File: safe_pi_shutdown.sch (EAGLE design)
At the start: 32 parts, among them IC1 MCP73831, IC2 LTC2952CF, IC3 MT3608, Q1 IRF7342, Q2 IRF7342, X4 22-27-2021-02

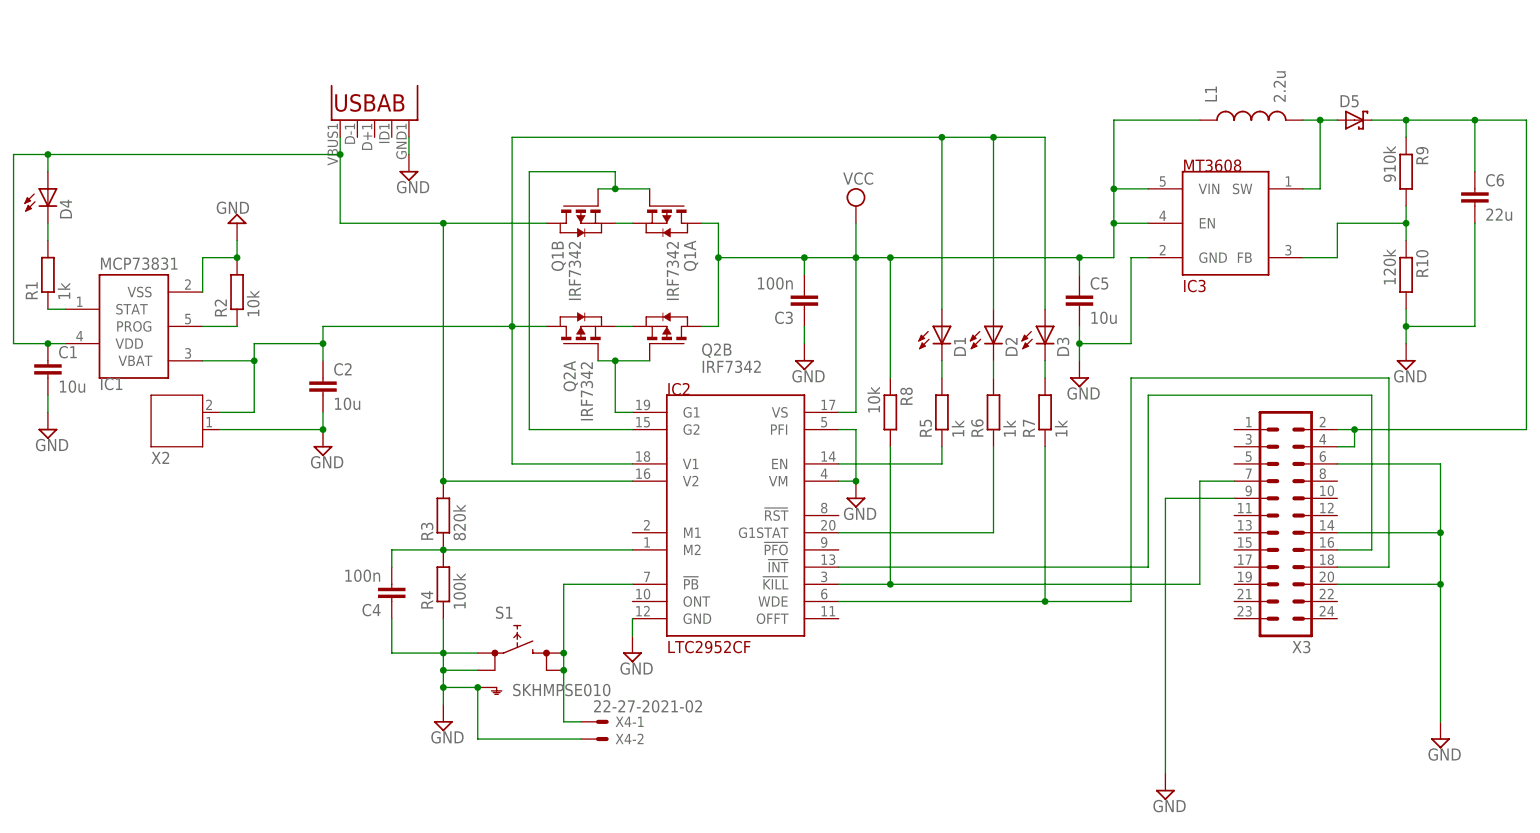
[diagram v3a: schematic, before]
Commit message: dodanie headerow do podlaczenia do plyty bazowej
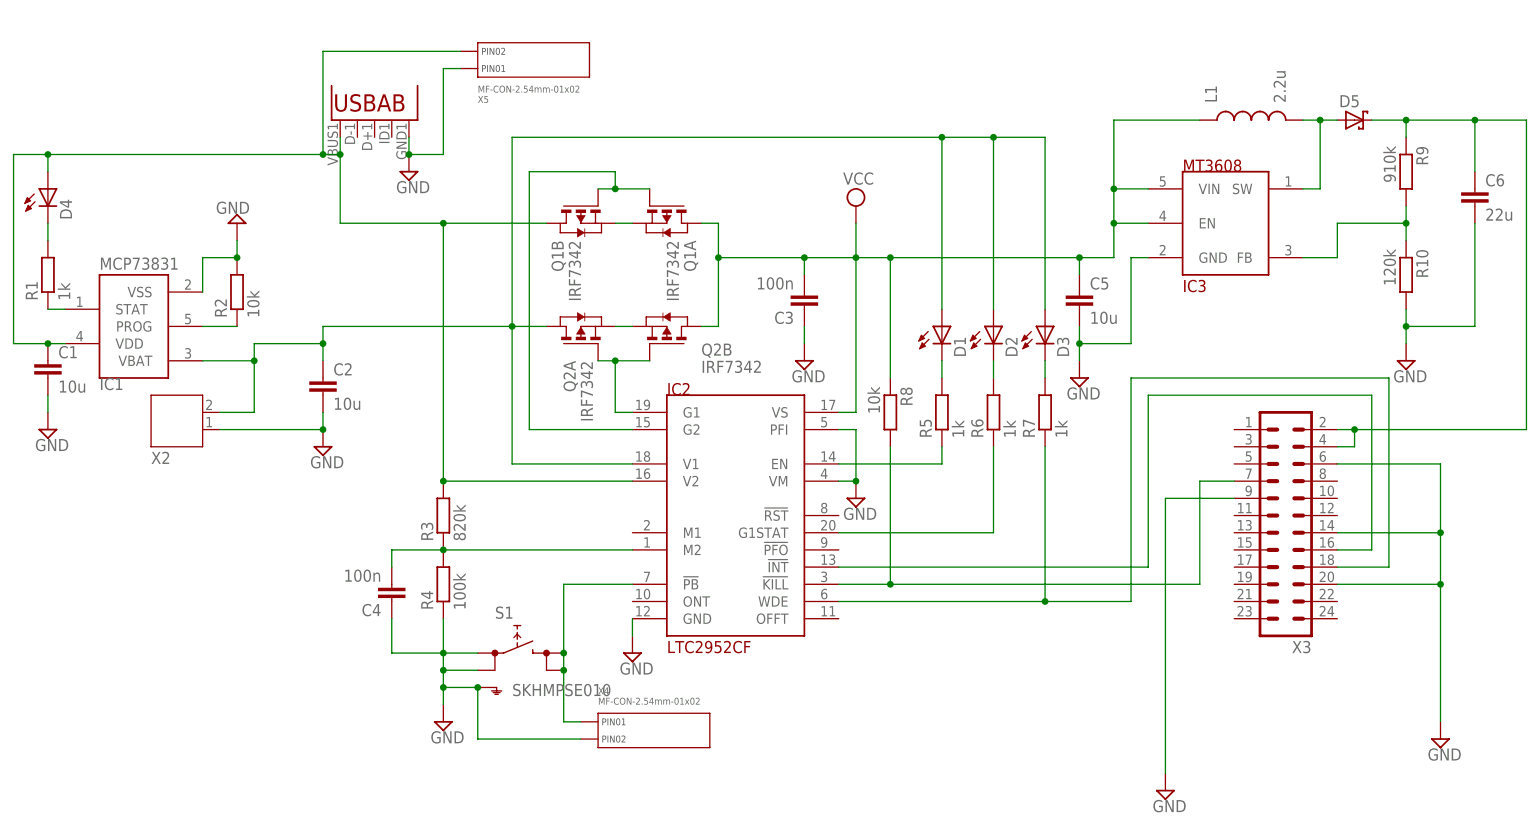
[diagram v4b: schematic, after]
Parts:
- added X5: MF-CON-2.54mm-01x02, MF_Connectors:CON_01X02_PTH_2.54MM
- X4: value 22-27-2021-02 -> MF-CON-2.54mm-01x02; device con-molex:22-27-2021-02 -> MF_Connectors:CON_01X02_PTH_2.54MM
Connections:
- net GND: now also X4.PIN2, X5.PIN1; no longer X4-2.S
- net N$5: now also X4.PIN1; no longer X4-1.S
- net V2: now also X5.PIN2
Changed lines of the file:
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@@
 <part name="IC1" library="mcp73831" deviceset="MCP73831" device=""/>
 <part name="SUPPLY14" library="supply2" deviceset="GND" device=""/>
-<part name="X4" library="con-molex" deviceset="22-?-02" device="27-2021"/>
 <part name="X3" library="con-lstb" deviceset="MA12-2" device=""/>
+<part name="X5" library="MF_Connectors" deviceset="CON_01X02" device="_PTH_2.54MM" value="MF-CON-2.54mm-01x02"/>
+<part name="X4" library="MF_Connectors" deviceset="CON_01X02" device="_PTH_2.54MM" value="MF-CON-2.54mm-01x02"/>
 </parts>
 <sheets>
@@
 <instance part="IC1" gate="G$1" x="22.86" y="139.7" rot="MR180"/>
 <instance part="SUPPLY14" gate="GND" x="10.16" y="124.46"/>
-<instance part="X4" gate="-1" x="91.44" y="81.28"/>
-<instance part="X4" gate="-2" x="91.44" y="78.74"/>
 <instance part="X3" gate="1" x="193.04" y="111.76" rot="R180"/>
+<instance part="X5" gate="G$1" x="73.66" y="177.8" rot="MR180"/>
+<instance part="X4" gate="G$1" x="91.44" y="81.28"/>
 </instances>
 <busses>
@@
 <wire x1="63.5" y1="167.64" x2="63.5" y2="165.1" width="0.1524" layer="91"/>
 <pinref part="SUPPLY1" gate="GND" pin="GND"/>
+<wire x1="63.5" y1="165.1" x2="68.58" y2="165.1" width="0.1524" layer="91"/>
+<wire x1="68.58" y1="165.1" x2="68.58" y2="177.8" width="0.1524" layer="91"/>
+<junction x="63.5" y="165.1"/>
+<pinref part="X5" gate="G$1" pin="PIN1"/>
+<wire x1="68.58" y1="177.8" x2="71.12" y2="177.8" width="0.1524" layer="91"/>
 </segment>
 <segment>
@@
 <wire x1="73.66" y1="78.74" x2="73.66" y2="86.36" width="0.1524" layer="91"/>
 <junction x="73.66" y="86.36"/>
-<pinref part="X4" gate="-2" pin="S"/>
+<pinref part="X4" gate="G$1" pin="PIN2"/>
 </segment>
 <segment>
@@
 <pinref part="D4" gate="G$1" pin="A"/>
 <wire x1="10.16" y1="162.56" x2="10.16" y2="165.1" width="0.1524" layer="91"/>
-<wire x1="10.16" y1="165.1" x2="53.34" y2="165.1" width="0.1524" layer="91"/>
+<wire x1="10.16" y1="165.1" x2="50.8" y2="165.1" width="0.1524" layer="91"/>
 <pinref part="IC1" gate="G$1" pin="VDD"/>
 <pinref part="C1" gate="G$1" pin="1"/>
+<wire x1="50.8" y1="165.1" x2="53.34" y2="165.1" width="0.1524" layer="91"/>
 <wire x1="12.7" y1="137.16" x2="10.16" y2="137.16" width="0.1524" layer="91"/>
 <wire x1="10.16" y1="137.16" x2="5.08" y2="137.16" width="0.1524" layer="91"/>
@@
 <junction x="10.16" y="165.1"/>
 <junction x="10.16" y="137.16"/>
+<wire x1="50.8" y1="165.1" x2="50.8" y2="180.34" width="0.1524" layer="91"/>
+<junction x="50.8" y="165.1"/>
+<pinref part="X5" gate="G$1" pin="PIN2"/>
+<wire x1="50.8" y1="180.34" x2="71.12" y2="180.34" width="0.1524" layer="91"/>
 </segment>
 </net>
@@
 <junction x="86.36" y="88.9"/>
 <junction x="86.36" y="91.44"/>
-<pinref part="X4" gate="-1" pin="S"/>
-</segment>
-</net>
+<pinref part="X4" gate="G$1" pin="PIN1"/>
+</segment>
+</net>

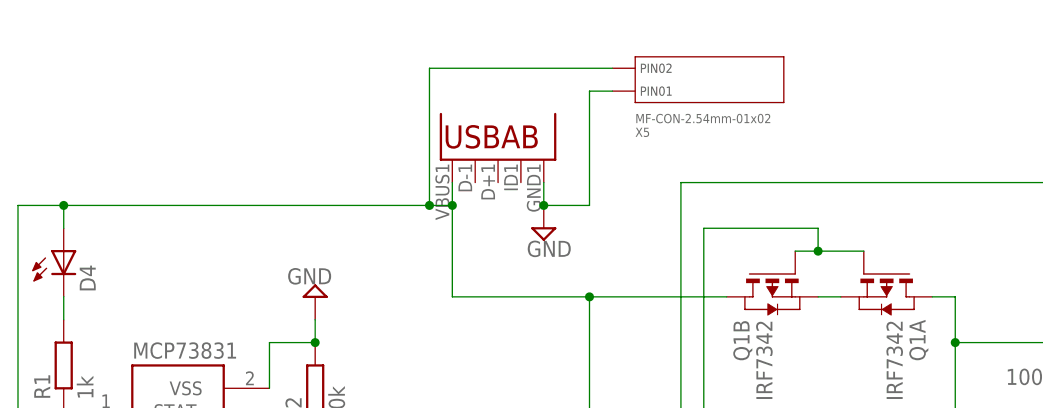
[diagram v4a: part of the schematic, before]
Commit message: zmiana micro usb, poprawki z kondensatorami i inne
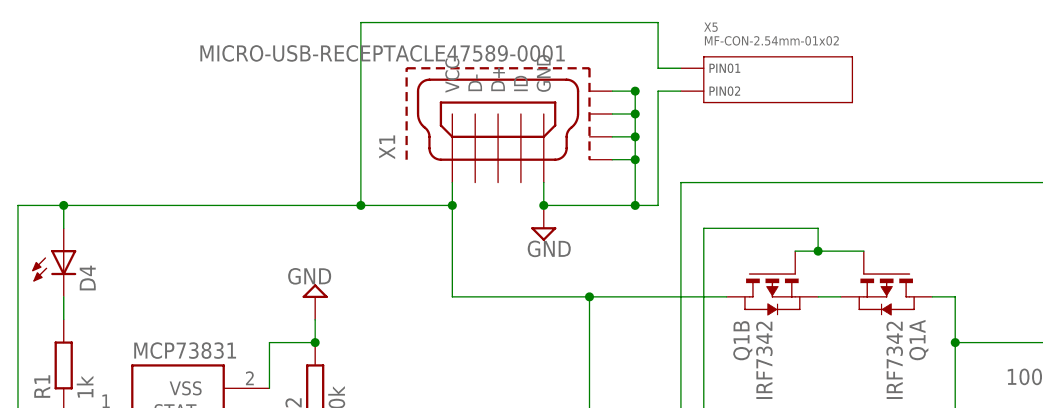
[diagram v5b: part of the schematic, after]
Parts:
- C5, C6: device rcl:C-EUC0603 -> rcl:C-EUC1206
- X1: value (none) -> MICRO-USB-RECEPTACLE47589-0001; device MicroUSB:USB"" -> con-molex-usb:MICRO-USB-RECEPTACLE47589-0001
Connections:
- net GND: now also X1.GND1, X1.GND2, X1.GND3, X1.GND4, X5.PIN2; no longer X5.PIN1
- net V2: now also X1.VCC, X5.PIN1; no longer X1.VBUS, X5.PIN2
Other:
- moved on the sheet: X5

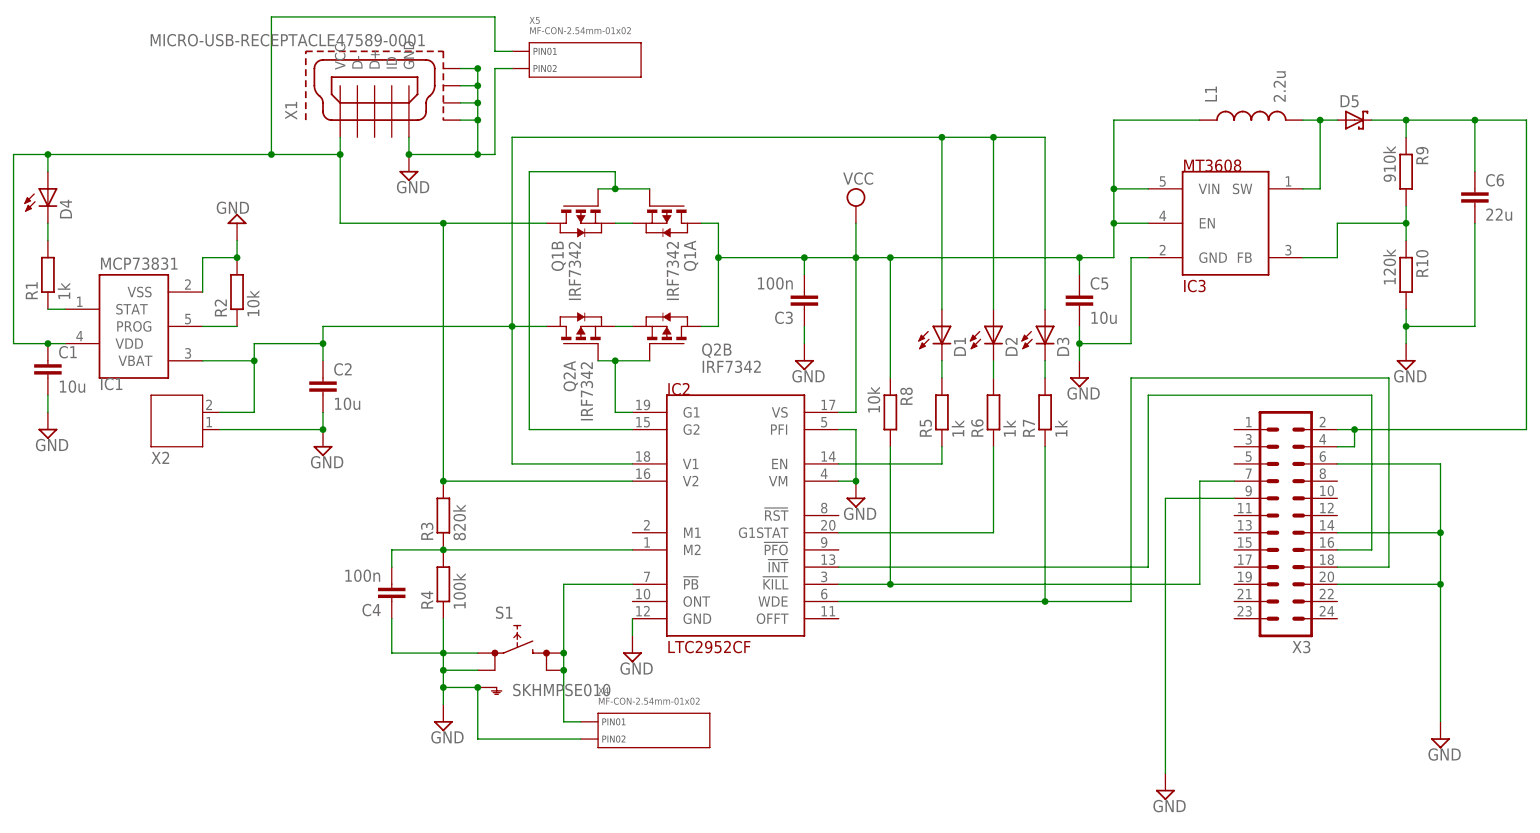
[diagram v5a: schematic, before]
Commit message: dodanie pull-up dla pinu INT
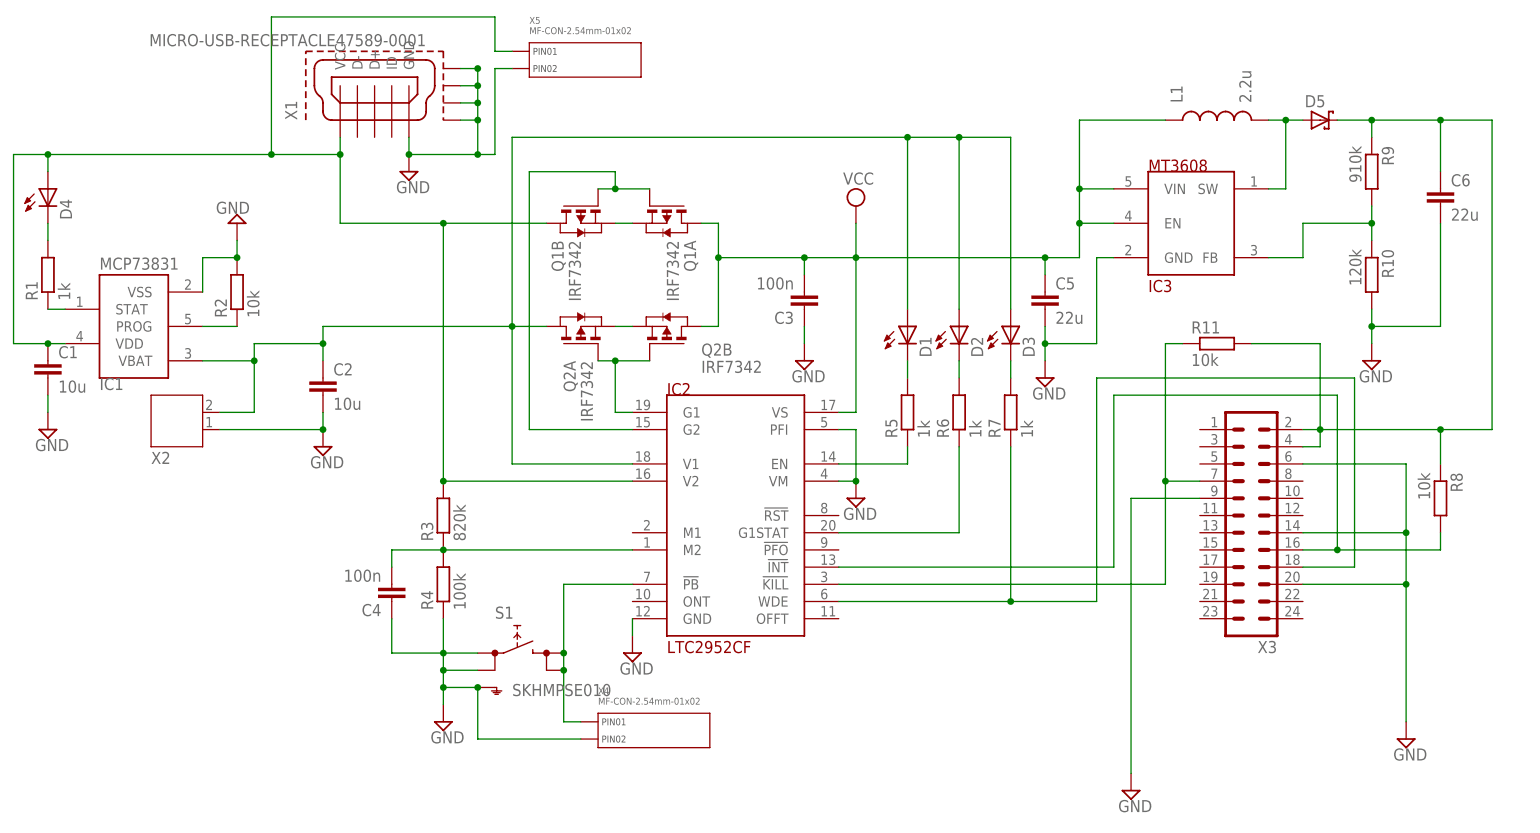
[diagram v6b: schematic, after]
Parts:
- added R11: 10k, rcl:R-EU_R0603
- C5: value 10u -> 22u
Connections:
- net N$10: now also R8.2
- net N$12: now also R11.1; no longer R8.2
- net N$4: now also R11.2, R8.1
- net VCC: no longer R8.1
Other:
- moved on the sheet: C5, C6, D1, D2, D3, D5, IC3, L1, R10, R5, R6, R7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

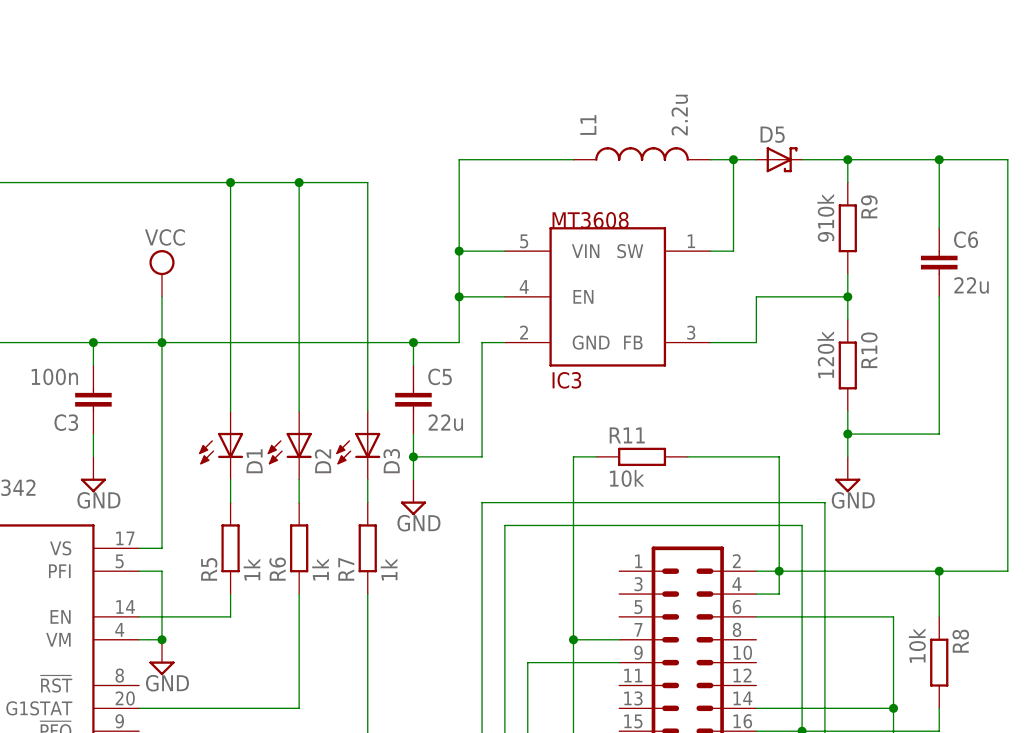
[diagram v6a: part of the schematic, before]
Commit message: boost converter changed to MIC2876
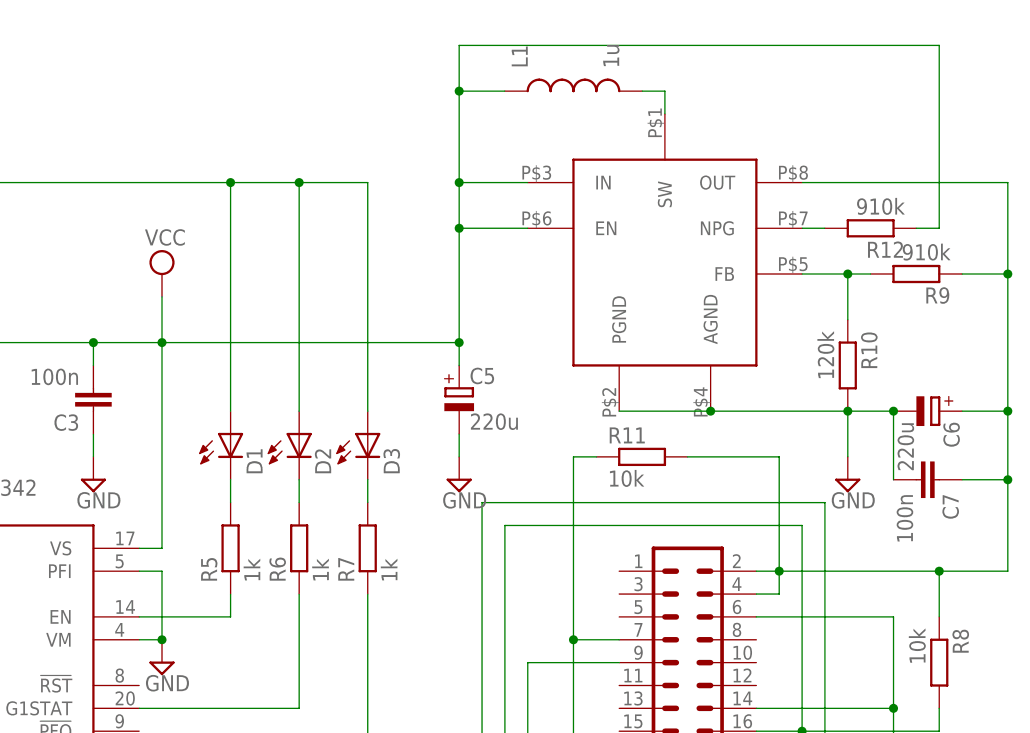
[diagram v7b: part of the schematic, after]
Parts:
- removed D5: (no value), eagle-ltspice:SCHOTTKY-DIODE
- added C7: 100n, rcl:C-EUC0402
- added R12: 910k, rcl:R-EU_R0603
- C5, C6: value 22u -> 220u; device rcl:C-EUC1206 -> rcl:CPOL-EUE3.5-8
- IC3: value MT3608 -> MIC2876; device mt3608:MT3608 -> mic2876:MIC2876
- L1: value 2.2u -> 1u; device SparkFun-Passives:INDUCTORDR1030 -> SparkFun-Passives:INDUCTORCR54-KIT
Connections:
- removed net N$13: D5.C, IC3.SW, L1.2
- new net N$11: IC3.NPG, R12.2
- new net N$9: IC3.SW, L1.2
- net GND: now also C5.-, C6.-, C7.2, IC3.AGND, IC3.PGND; no longer C5.2, C6.2, IC3.GND
- net N$4: now also C6.+, C7.1, IC3.OUT; no longer C6.1, D5.A
- net VCC: now also C5.+, IC3.IN, R12.1; no longer C5.1, IC3.VIN
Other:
- moved on the sheet: L1, R9
